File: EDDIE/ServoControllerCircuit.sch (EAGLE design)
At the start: 31 parts, among them Q1 20MHz, T1 2N3904, X1 SIGNAL-PWR-GND, X2 SIGNAL-PWR-GND

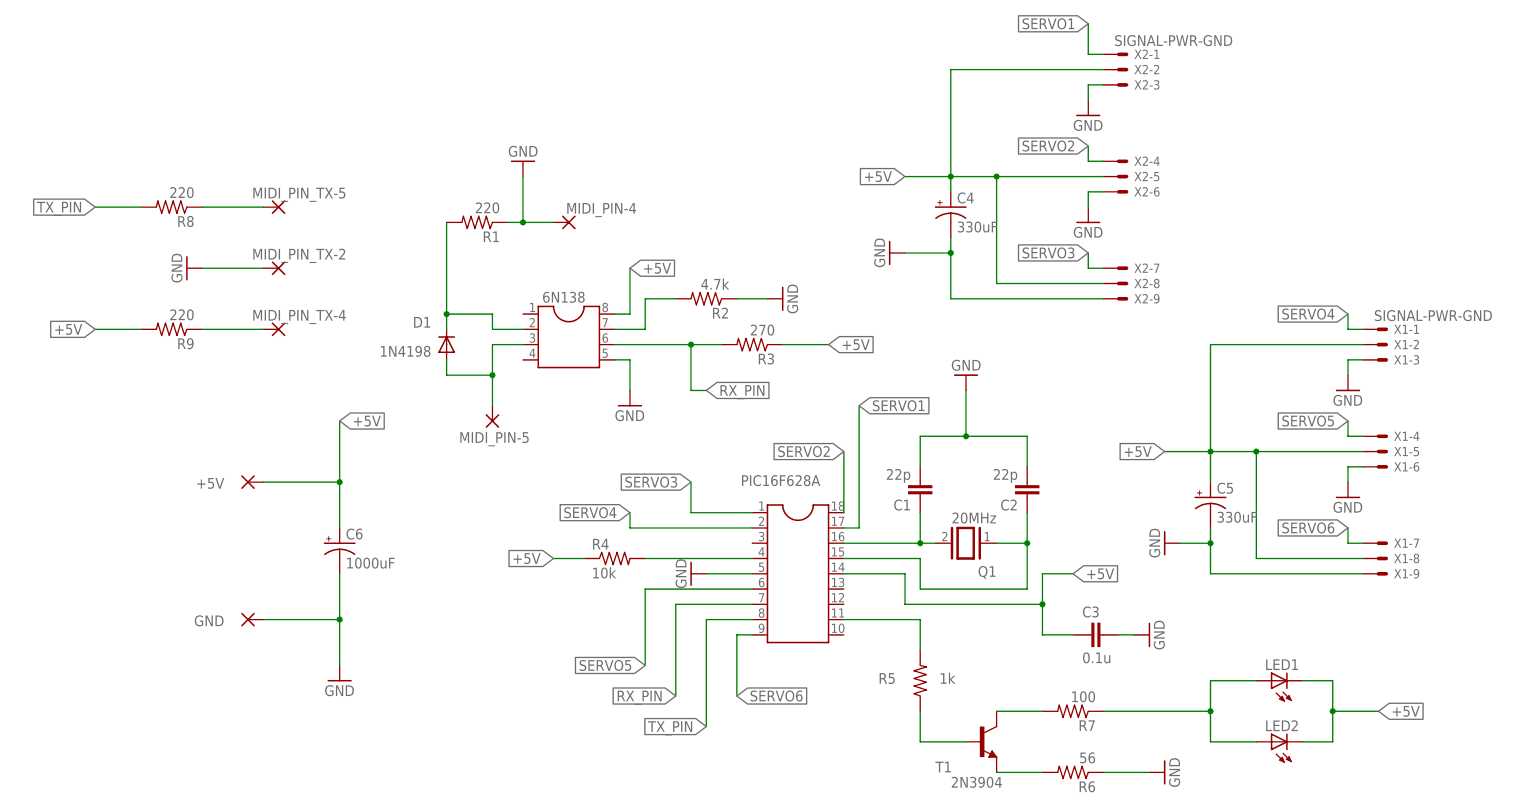
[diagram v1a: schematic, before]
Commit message: Removed TX circuitry and moved cost analysis
Since the TX functionality for the PIC was not tested, I decided to remove it. It is also the case that the cost analysis file for Jim, which is currently in progress, was moved to the Document repository.
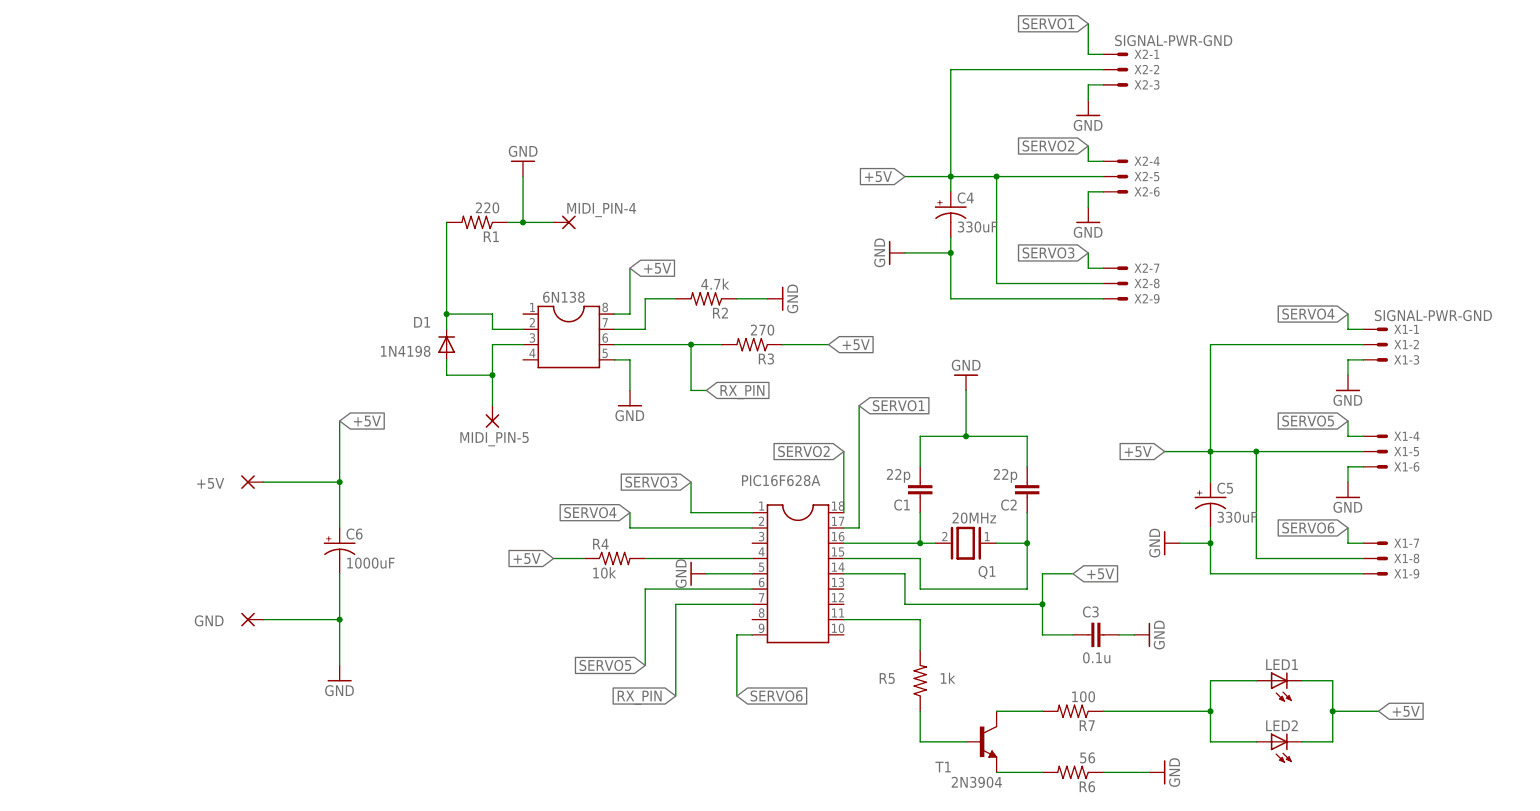
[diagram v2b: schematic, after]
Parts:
- removed MIDI_PIN_TX-2, MIDI_PIN_TX-4, MIDI_PIN_TX-5: (no value), wirepad:2,15/1,0
- removed R8, R9: 220, resistor:R-US_0207/12
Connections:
- removed net N$11: MIDI_PIN_TX-5.P, R8.1
- removed net N$12: MIDI_PIN_TX-4.P, R9.1
- removed net TX_PIN: PIC16F628A.8, R8.2
- net +5V: no longer R9.2
- net GND: no longer MIDI_PIN_TX-2.P
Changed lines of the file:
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@@
 <?xml version="1.0" encoding="utf-8"?>
 <!DOCTYPE eagle SYSTEM "eagle.dtd">
-<eagle version="8.6.1">
+<eagle version="8.6.3">
 <drawing>
 <settings>
@@
 <part name="+5V" library="wirepad" deviceset="2,15/1,0" device=""/>
 <part name="T1" library="transistor" deviceset="2N3904" device=""/>
-<part name="MIDI_PIN_TX-4" library="wirepad" deviceset="2,15/1,0" device=""/>
-<part name="MIDI_PIN_TX-5" library="wirepad" deviceset="2,15/1,0" device=""/>
-<part name="MIDI_PIN_TX-2" library="wirepad" deviceset="2,15/1,0" device=""/>
-<part name="GND12" library="supply1" deviceset="GND" device=""/>
-<part name="R8" library="resistor" deviceset="R-US_" device="0207/12" value="220"/>
-<part name="R9" library="resistor" deviceset="R-US_" device="0207/12" value="220"/>
 <part name="C6" library="resistor" deviceset="CPOL-US" device="E5-10.5" value="1000uF"/>
 <part name="C4" library="resistor" deviceset="CPOL-US" device="E3.5-8" value="330uF"/>
@@
 <attribute name="VALUE" x="88.9" y="-12.7" size="1.778" layer="96"/>
 </instance>
-<instance part="MIDI_PIN_TX-4" gate="1" x="-22.86" y="63.5" smashed="yes" rot="R180">
-<attribute name="NAME" x="-11.557" y="66.7258" size="1.778" layer="95" rot="R180"/>
-<attribute name="VALUE" x="-21.717" y="66.802" size="1.778" layer="96" rot="R180"/>
-</instance>
-<instance part="MIDI_PIN_TX-5" gate="1" x="-22.86" y="83.82" smashed="yes" rot="R180">
-<attribute name="NAME" x="-11.557" y="87.0458" size="1.778" layer="95" rot="R180"/>
-<attribute name="VALUE" x="-21.717" y="87.122" size="1.778" layer="96" rot="R180"/>
-</instance>
-<instance part="MIDI_PIN_TX-2" gate="1" x="-22.86" y="73.66" smashed="yes" rot="R180">
-<attribute name="NAME" x="-11.557" y="76.8858" size="1.778" layer="95" rot="R180"/>
-<attribute name="VALUE" x="-21.717" y="76.962" size="1.778" layer="96" rot="R180"/>
-</instance>
-<instance part="GND12" gate="1" x="-38.1" y="73.66" rot="R270"/>
-<instance part="R8" gate="G$1" x="-40.64" y="83.82" rot="R180"/>
-<instance part="R9" gate="G$1" x="-40.64" y="63.5" rot="R180"/>
 <instance part="C6" gate="G$1" x="-12.7" y="27.94"/>
 <instance part="C4" gate="G$1" x="88.9" y="83.82"/>
@@
 <label x="160.02" y="0" size="1.778" layer="95" xref="yes"/>
 </segment>
-<segment>
-<pinref part="R9" gate="G$1" pin="2"/>
-<wire x1="-45.72" y1="63.5" x2="-53.34" y2="63.5" width="0.1524" layer="91"/>
-<label x="-53.34" y="63.5" size="1.778" layer="95" rot="R180" xref="yes"/>
-</segment>
 </net>
 <net name="N$2" class="0">
@@
 <junction x="88.9" y="76.2"/>
 <pinref part="C4" gate="G$1" pin="-"/>
-</segment>
-<segment>
-<pinref part="MIDI_PIN_TX-2" gate="1" pin="P"/>
-<wire x1="-25.4" y1="73.66" x2="-35.56" y2="73.66" width="0.1524" layer="91"/>
-<pinref part="GND12" gate="1" pin="GND"/>
 </segment>
 </net>
@@
 </segment>
 </net>
-<net name="TX_PIN" class="0">
-<segment>
-<pinref part="PIC16F628A" gate="G$1" pin="8"/>
-<wire x1="55.88" y1="15.24" x2="48.26" y2="15.24" width="0.1524" layer="91"/>
-<wire x1="48.26" y1="15.24" x2="48.26" y2="-2.54" width="0.1524" layer="91"/>
-<label x="48.26" y="-2.54" size="1.778" layer="95" rot="R180" xref="yes"/>
-</segment>
-<segment>
-<pinref part="R8" gate="G$1" pin="2"/>
-<wire x1="-45.72" y1="83.82" x2="-53.34" y2="83.82" width="0.1524" layer="91"/>
-<label x="-53.34" y="83.82" size="1.778" layer="95" rot="R180" xref="yes"/>
-</segment>
-</net>
-<net name="N$11" class="0">
-<segment>
-<pinref part="MIDI_PIN_TX-5" gate="1" pin="P"/>
-<wire x1="-25.4" y1="83.82" x2="-35.56" y2="83.82" width="0.1524" layer="91"/>
-<pinref part="R8" gate="G$1" pin="1"/>
-</segment>
-</net>
-<net name="N$12" class="0">
-<segment>
-<pinref part="MIDI_PIN_TX-4" gate="1" pin="P"/>
-<wire x1="-25.4" y1="63.5" x2="-35.56" y2="63.5" width="0.1524" layer="91"/>
-<pinref part="R9" gate="G$1" pin="1"/>
-</segment>
-</net>
